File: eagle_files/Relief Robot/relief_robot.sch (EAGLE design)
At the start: 38 parts, among them IC2 7805T, U2 FT232RLSSOP, U3 ATMEGA328P_PDIP, U4 JOYSTICKPTH, X2 USB-SMD-NS

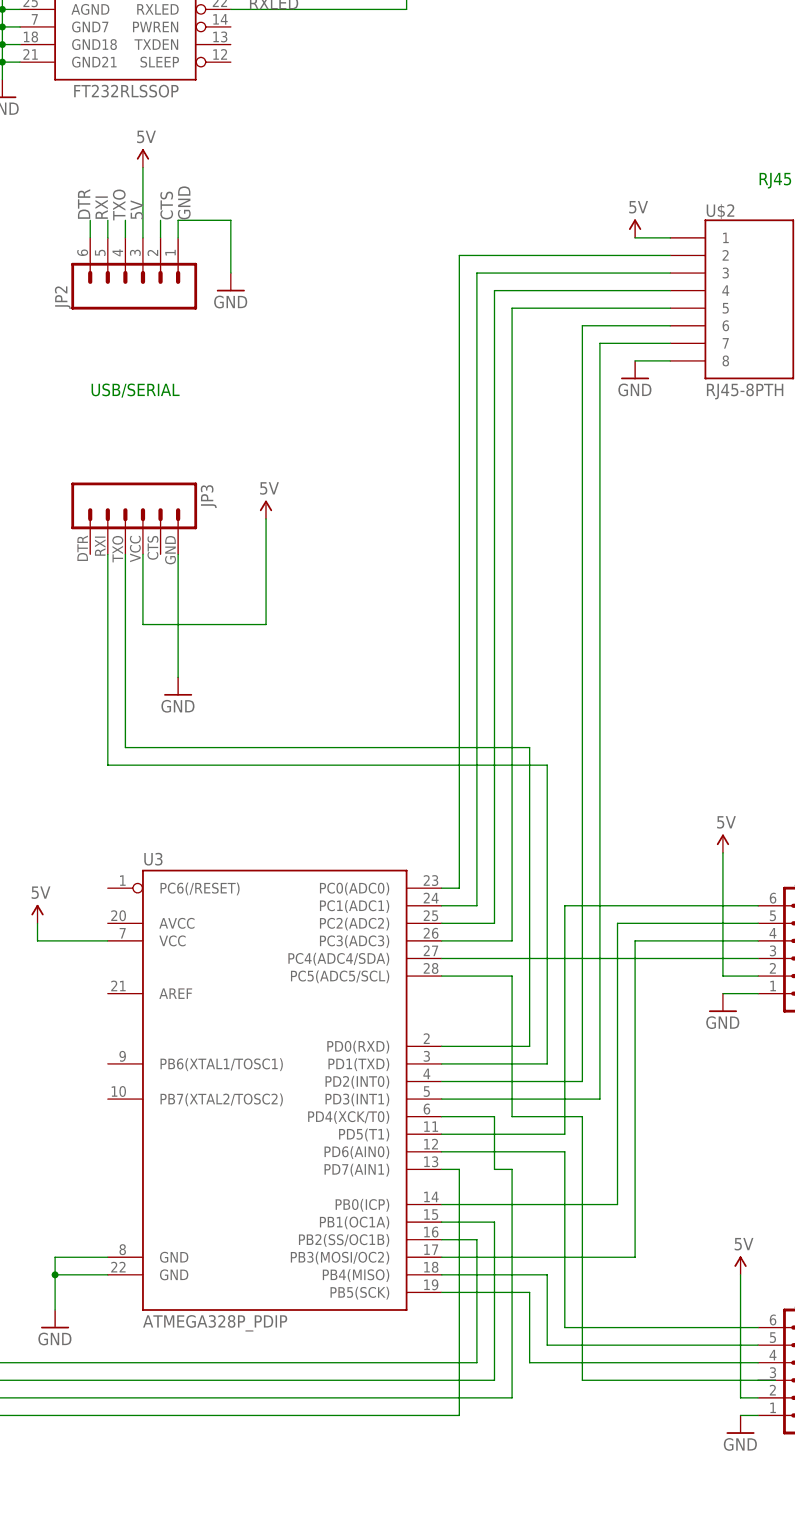
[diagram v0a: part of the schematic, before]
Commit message: created controller read test modules
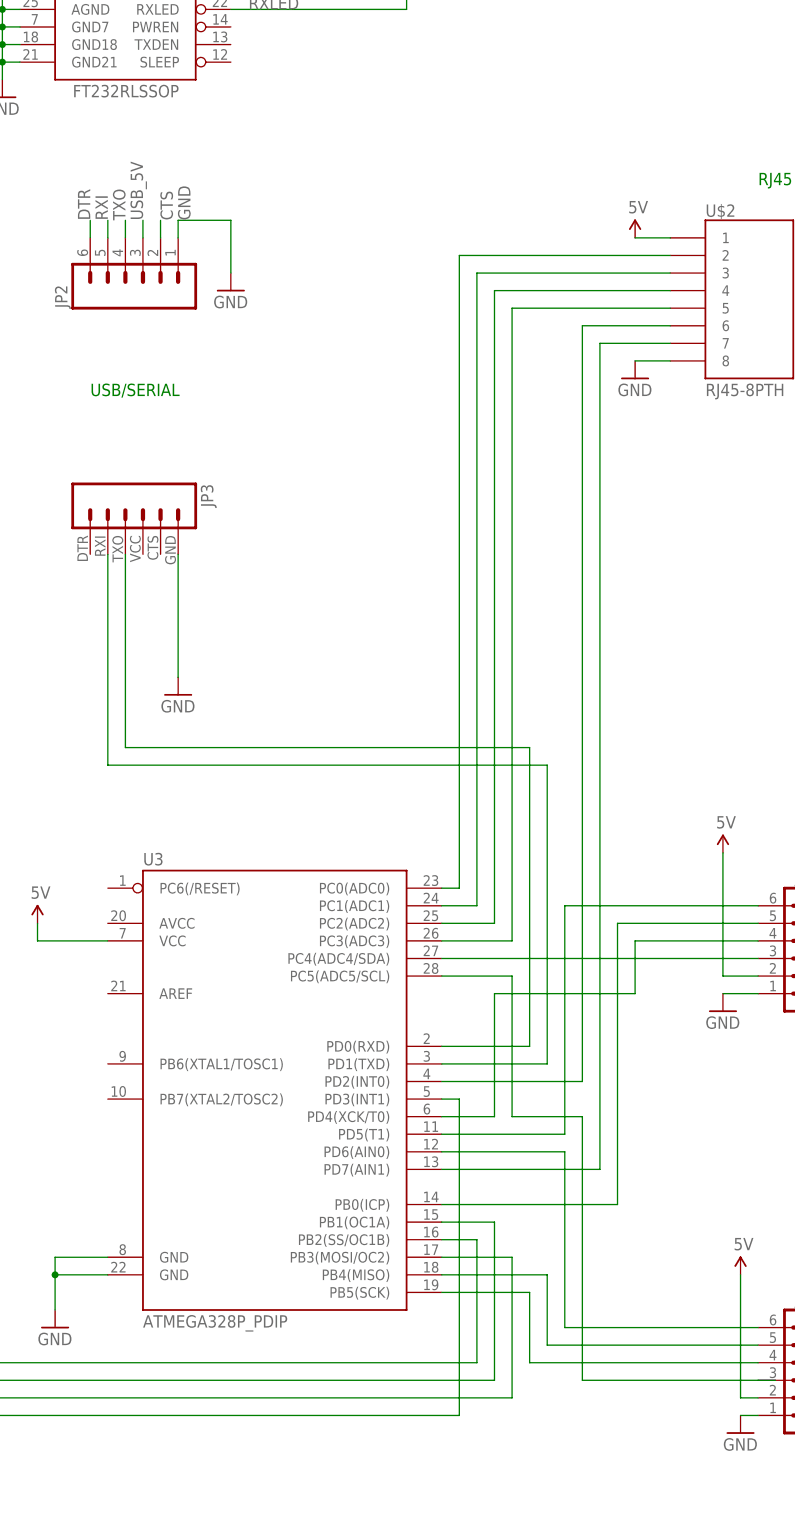
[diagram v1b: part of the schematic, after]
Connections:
- removed net N$32: JP7.2, U3.PD7(AIN1)
- new net N$6: JP6.2, U3.PB3(MOSI/OC2)
- new net USB_5V: JP2.3
- net 5V: no longer JP2.3, JP3.4
- net N$24: now also JP7.2; no longer U$2.7
- net N$27: now also JP19.4; no longer JP6.2
- net N$31: now also U$2.7, U3.PD7(AIN1); no longer JP19.4, U3.PB3(MOSI/OC2)
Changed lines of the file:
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@@
 <?xml version="1.0" encoding="utf-8"?>
 <!DOCTYPE eagle SYSTEM "eagle.dtd">
-<eagle version="6.5.0">
+<eagle version="6.4">
 <drawing>
 <settings>
@@
 <part name="U$5" library="SparkFun" deviceset="5V" device=""/>
 <part name="JP2" library="SparkFun" deviceset="M06" device="SMD-FEMALE-V2"/>
-<part name="SUPPLY6" library="SparkFun-Aesthetics" deviceset="5V" device=""/>
 <part name="JP3" library="SparkFun-Connectors" deviceset="M06" device="SIP"/>
 <part name="IC2" library="adafruit" deviceset="78*" device="T" technology="05"/>
@@
 <part name="SUPPLY9" library="SparkFun-Aesthetics" deviceset="5V" device=""/>
 <part name="GND17" library="SparkFun-Aesthetics" deviceset="GND" device=""/>
-<part name="SUPPLY10" library="SparkFun-Aesthetics" deviceset="5V" device=""/>
 <part name="GND18" library="SparkFun-Aesthetics" deviceset="GND" device=""/>
 <part name="U$6" library="SparkFun-Electromechanical" deviceset="MOTOR" device="10MM" value="MOTOR_100:1"/>
@@
 <instance part="U$5" gate="G$1" x="68.58" y="233.68"/>
 <instance part="JP2" gate="G$1" x="30.48" y="167.64" rot="R90"/>
-<instance part="SUPPLY6" gate="G$1" x="30.48" y="182.88"/>
 <instance part="JP3" gate="G$1" x="27.94" y="132.08" rot="R270"/>
 <instance part="IC2" gate="A1" x="-27.94" y="106.68"/>
@@
 <instance part="SUPPLY9" gate="G$1" x="-10.16" y="109.22"/>
 <instance part="GND17" gate="1" x="-27.94" y="93.98"/>
-<instance part="SUPPLY10" gate="G$1" x="48.26" y="132.08"/>
 <instance part="GND18" gate="1" x="35.56" y="106.68"/>
 <instance part="U$6" gate="G$1" x="299.72" y="76.2"/>
@@
 </segment>
 <segment>
-<wire x1="30.48" y1="172.72" x2="30.48" y2="182.88" width="0.1524" layer="91"/>
-<label x="30.48" y="175.26" size="1.778" layer="95" rot="R90"/>
-<pinref part="JP2" gate="G$1" pin="3"/>
-<pinref part="SUPPLY6" gate="G$1" pin="5V"/>
-</segment>
-<segment>
 <pinref part="SUPPLY9" gate="G$1" pin="5V"/>
 <pinref part="IC2" gate="A1" pin="VO"/>
 <wire x1="-10.16" y1="109.22" x2="-10.16" y2="106.68" width="0.1524" layer="91"/>
 <wire x1="-10.16" y1="106.68" x2="-17.78" y2="106.68" width="0.1524" layer="91"/>
-</segment>
-<segment>
-<pinref part="JP3" gate="G$1" pin="4"/>
-<wire x1="30.48" y1="127" x2="30.48" y2="116.84" width="0.1524" layer="91"/>
-<wire x1="30.48" y1="116.84" x2="48.26" y2="116.84" width="0.1524" layer="91"/>
-<pinref part="SUPPLY10" gate="G$1" pin="5V"/>
-<wire x1="48.26" y1="116.84" x2="48.26" y2="132.08" width="0.1524" layer="91"/>
 </segment>
 <segment>
@@
 </segment>
 </net>
-<net name="N$24" class="0">
-<segment>
-<pinref part="U$2" gate="G$1" pin="7"/>
-<wire x1="106.68" y1="157.48" x2="96.52" y2="157.48" width="0.1524" layer="91"/>
-<wire x1="96.52" y1="157.48" x2="96.52" y2="48.26" width="0.1524" layer="91"/>
-<pinref part="U3" gate="G$1" pin="PD3(INT1)"/>
-<wire x1="96.52" y1="48.26" x2="73.66" y2="48.26" width="0.1524" layer="91"/>
-</segment>
-</net>
 <net name="N$25" class="0">
 <segment>
@@
 <wire x1="88.9" y1="12.7" x2="119.38" y2="12.7" width="0.1524" layer="91"/>
 <pinref part="JP12" gate="G$1" pin="5"/>
-</segment>
-</net>
-<net name="N$27" class="0">
-<segment>
-<pinref part="U3" gate="G$1" pin="PD4(XCK/T0)"/>
-<wire x1="73.66" y1="45.72" x2="81.28" y2="45.72" width="0.1524" layer="91"/>
-<wire x1="81.28" y1="45.72" x2="81.28" y2="38.1" width="0.1524" layer="91"/>
-<wire x1="81.28" y1="38.1" x2="83.82" y2="38.1" width="0.1524" layer="91"/>
-<wire x1="83.82" y1="38.1" x2="83.82" y2="5.08" width="0.1524" layer="91"/>
-<wire x1="83.82" y1="5.08" x2="-7.62" y2="5.08" width="0.1524" layer="91"/>
-<wire x1="-7.62" y1="5.08" x2="-7.62" y2="25.4" width="0.1524" layer="91"/>
-<pinref part="JP6" gate="G$1" pin="2"/>
-<wire x1="-7.62" y1="25.4" x2="-40.64" y2="25.4" width="0.1524" layer="91"/>
-</segment>
-</net>
-<net name="N$32" class="0">
-<segment>
-<pinref part="U3" gate="G$1" pin="PD7(AIN1)"/>
-<wire x1="73.66" y1="38.1" x2="76.2" y2="38.1" width="0.1524" layer="91"/>
-<wire x1="76.2" y1="38.1" x2="76.2" y2="2.54" width="0.1524" layer="91"/>
-<wire x1="76.2" y1="2.54" x2="-40.64" y2="2.54" width="0.1524" layer="91"/>
-<pinref part="JP7" gate="G$1" pin="2"/>
 </segment>
 </net>
@@
 <pinref part="JP10" gate="G$1" pin="2"/>
 <wire x1="220.98" y1="78.74" x2="241.3" y2="78.74" width="0.1524" layer="91"/>
-</segment>
-</net>
-<net name="N$31" class="0">
-<segment>
-<pinref part="U3" gate="G$1" pin="PB3(MOSI/OC2)"/>
-<wire x1="73.66" y1="25.4" x2="101.6" y2="25.4" width="0.1524" layer="91"/>
-<wire x1="101.6" y1="25.4" x2="101.6" y2="71.12" width="0.1524" layer="91"/>
-<wire x1="101.6" y1="71.12" x2="119.38" y2="71.12" width="0.1524" layer="91"/>
-<pinref part="JP19" gate="G$1" pin="4"/>
 </segment>
 </net>
@@
 </segment>
 </net>
+<net name="N$6" class="0">
+<segment>
+<pinref part="U3" gate="G$1" pin="PB3(MOSI/OC2)"/>
+<wire x1="73.66" y1="25.4" x2="83.82" y2="25.4" width="0.1524" layer="91"/>
+<wire x1="83.82" y1="25.4" x2="83.82" y2="5.08" width="0.1524" layer="91"/>
+<wire x1="83.82" y1="5.08" x2="-7.62" y2="5.08" width="0.1524" layer="91"/>
+<wire x1="-7.62" y1="5.08" x2="-7.62" y2="25.4" width="0.1524" layer="91"/>
+<pinref part="JP6" gate="G$1" pin="2"/>
+<wire x1="-7.62" y1="25.4" x2="-40.64" y2="25.4" width="0.1524" layer="91"/>
+</segment>
+</net>
+<net name="N$27" class="0">
+<segment>
+<pinref part="U3" gate="G$1" pin="PD4(XCK/T0)"/>
+<wire x1="73.66" y1="45.72" x2="81.28" y2="45.72" width="0.1524" layer="91"/>
+<wire x1="81.28" y1="45.72" x2="81.28" y2="63.5" width="0.1524" layer="91"/>
+<wire x1="81.28" y1="63.5" x2="101.6" y2="63.5" width="0.1524" layer="91"/>
+<wire x1="101.6" y1="63.5" x2="101.6" y2="71.12" width="0.1524" layer="91"/>
+<pinref part="JP19" gate="G$1" pin="4"/>
+<wire x1="101.6" y1="71.12" x2="119.38" y2="71.12" width="0.1524" layer="91"/>
+</segment>
+</net>
+<net name="N$24" class="0">
+<segment>
+<pinref part="U3" gate="G$1" pin="PD3(INT1)"/>
+<wire x1="73.66" y1="48.26" x2="76.2" y2="48.26" width="0.1524" layer="91"/>
+<wire x1="76.2" y1="48.26" x2="76.2" y2="2.54" width="0.1524" layer="91"/>
+<pinref part="JP7" gate="G$1" pin="2"/>
+<wire x1="76.2" y1="2.54" x2="-40.64" y2="2.54" width="0.1524" layer="91"/>
+</segment>
+</net>
+<net name="N$31" class="0">
+<segment>
+<pinref part="U3" gate="G$1" pin="PD7(AIN1)"/>
+<wire x1="73.66" y1="38.1" x2="96.52" y2="38.1" width="0.1524" layer="91"/>
+<wire x1="96.52" y1="38.1" x2="96.52" y2="157.48" width="0.1524" layer="91"/>
+<pinref part="U$2" gate="G$1" pin="7"/>
+<wire x1="96.52" y1="157.48" x2="106.68" y2="157.48" width="0.1524" layer="91"/>
+</segment>
+</net>
+<net name="USB_5V" class="0">
+<segment>
+<wire x1="30.48" y1="172.72" x2="30.48" y2="175.26" width="0.1524" layer="91"/>
+<label x="30.48" y="175.26" size="1.778" layer="95" rot="R90"/>
+<pinref part="JP2" gate="G$1" pin="3"/>
+</segment>
+</net>

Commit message: latest version of working code
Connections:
- net N$20: now also U3.PD5(T1); no longer U3.PD6(AIN0)
- net N$9: now also U3.PD6(AIN0); no longer U3.PD5(T1)
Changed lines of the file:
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@@
 <net name="N$20" class="0">
 <segment>
-<pinref part="U3" gate="G$1" pin="PD6(AIN0)"/>
-<wire x1="73.66" y1="40.64" x2="91.44" y2="40.64" width="0.1524" layer="91"/>
-<wire x1="91.44" y1="40.64" x2="91.44" y2="15.24" width="0.1524" layer="91"/>
 <wire x1="91.44" y1="15.24" x2="119.38" y2="15.24" width="0.1524" layer="91"/>
 <pinref part="JP12" gate="G$1" pin="6"/>
+<wire x1="91.44" y1="15.24" x2="91.44" y2="30.48" width="0.1524" layer="91"/>
+<wire x1="91.44" y1="30.48" x2="83.82" y2="30.48" width="0.1524" layer="91"/>
+<wire x1="83.82" y1="30.48" x2="83.82" y2="43.18" width="0.1524" layer="91"/>
+<pinref part="U3" gate="G$1" pin="PD5(T1)"/>
+<wire x1="83.82" y1="43.18" x2="73.66" y2="43.18" width="0.1524" layer="91"/>
 </segment>
 </net>
@@
 <segment>
 <wire x1="91.44" y1="76.2" x2="91.44" y2="43.18" width="0.1524" layer="91"/>
-<pinref part="U3" gate="G$1" pin="PD5(T1)"/>
-<wire x1="91.44" y1="43.18" x2="73.66" y2="43.18" width="0.1524" layer="91"/>
 <wire x1="91.44" y1="76.2" x2="119.38" y2="76.2" width="0.1524" layer="91"/>
 <pinref part="JP19" gate="G$1" pin="6"/>
+<pinref part="U3" gate="G$1" pin="PD6(AIN0)"/>
+<wire x1="73.66" y1="40.64" x2="86.36" y2="40.64" width="0.1524" layer="91"/>
+<wire x1="86.36" y1="40.64" x2="86.36" y2="43.18" width="0.1524" layer="91"/>
+<wire x1="86.36" y1="43.18" x2="91.44" y2="43.18" width="0.1524" layer="91"/>
 </segment>
 </net>
